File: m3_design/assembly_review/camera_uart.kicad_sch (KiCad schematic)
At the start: 13 parts, among them U12 TXU0202DCUR, U13 TPS70933DBVR

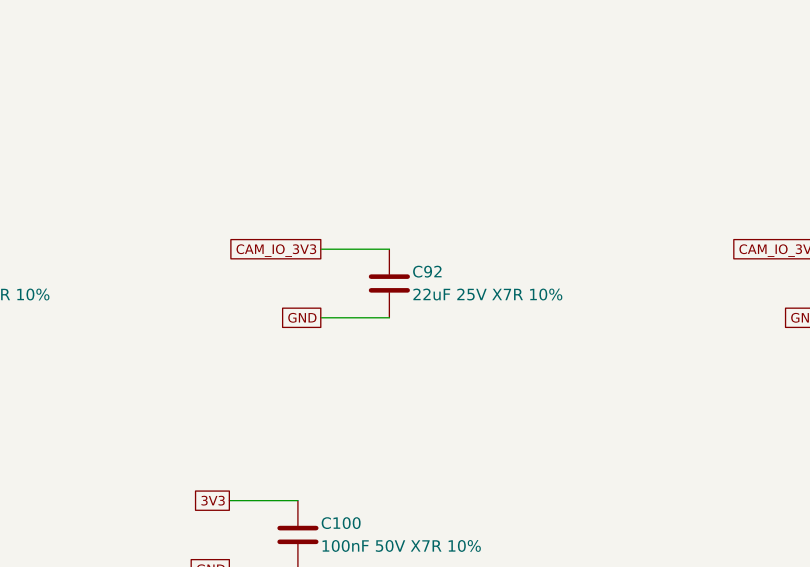
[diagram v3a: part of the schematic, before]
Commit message: R10 requirements-audit cuts and GAP fixes before review round 9
Implement adopted AUD-1 through AUD-10 and GAP-1 through GAP-5 after the single-switch pass.
Remove the advisory pull-pin, redundant probes and GPS/radio IO LDO cells; qualify the smaller
AONR21357 pair, correct C120 voltage rating, standardize shared-code capacitor lands, simplify
slow returns and fire-only copper, localize U9 output protection and add exactly two U401 VIPPO vias.
Record physical-current timing, coupled fire/source budget, C84 manual fitting and narrowed gate scopes.

Board SHA-256: 877d01996a59e9dd5c6dbc367274bb9a323a13982d67960fe46df9b0ee53205d
Board: 46 x 90 mm, 4 layers, 2365477 bytes; 225 footprints, 883 straight tracks, 323 vias.
Netlist SHA-256: 0843da709e2d7a757e9b35cdff48158a54012c5353619cbf409ab961efd2c3ca
Two fresh complete passing builds are byte-identical. Schematic: 700 pins; 22 seeded faults detected.

Final unskipped tools/check.sh: exit 0
DRC violations 0  unconnected 0  schematic parity 0  ERC 0
metadata / 3D model audit: OK
silkscreen outside the board outline: 0 stroke points
fit check: OK (CAD envelopes only)
R10 CAD contract (full): OK
routing hygiene: 0 failing, 0 allowlisted, 0 leftovers recorded
actuator safety contract: OK
Fab manifest: OK; 5 outputs match current CAD and export inputs
Self-tests: shell 4, fit 24, paste 5, routing 59, R10 131; three NumPy cases rerun and passed.

Fab: 215 CPL rows, 82 BOM codes; orientation / paste / manifest pass. Hot-plug: 2304 required
cases plus convergence and controls pass (simulation / Inference). Plate f1 280.9 Hz (Inference).
Live JLC: $84.43 vs $84.41 target, 46 Extended codes; R430 / U4 short. Procurement exit 1 is a
disclosed OQ-3 / ordering deviation, not a CAD gate pass. No quote accepted or order placed.
Firmware, bench, thermal/transient correlation, process acceptance, installed RF immunity and physical fit unverified.

This preparatory pass earns no clean-review credit. Start fresh full ten-lens round 9 on th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
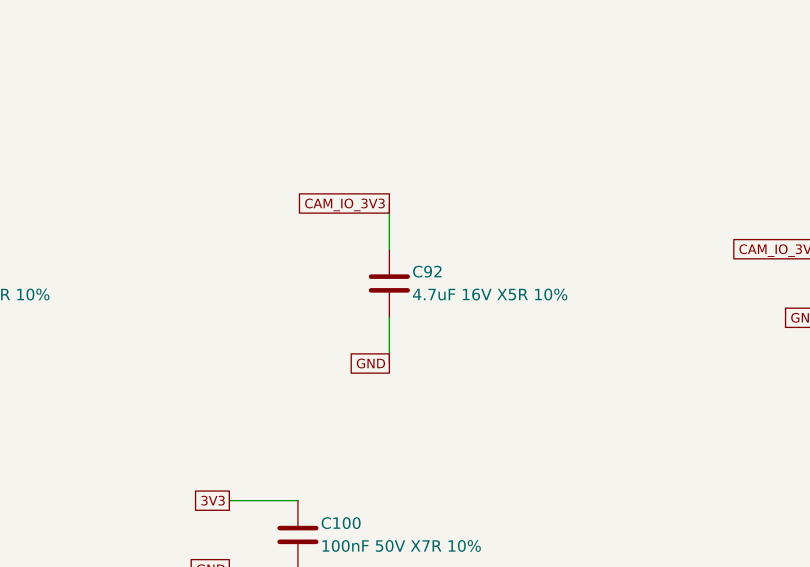
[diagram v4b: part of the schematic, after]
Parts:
- C92: value 22uF 25V X7R 10% -> 4.7uF 16V X5R 10%; footprint rocket:M3_GRM32_1210 -> rocket:C0603; LCSC C21397 -> C19666; LCSC Part C21397 -> (none); Manufacturer Murata -> Samsung Electro-Mechanics; Manufacturer Part GRM32ER71E226KE15L -> CL10A475KO8NNNC
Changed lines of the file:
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@@
+	(symbol
+		(lib_id "M3:C")
+		(at 269.24 137.16 0)
+		(unit 1)
+		(in_bom yes)
+		(on_board yes)
+		(dnp no)
+		(property "Reference" "C93"
+			(at 271.78000000000003 135.89 0)
+			(effects
+				(font
+					(size 1.27 1.27))
+				(justify left)))
+		(property "Value" "100nF 50V X7R 10%"
+			(at 271.78000000000003 138.42999999999998 0)
+			(effects
+				(font
+					(size 1.27 1.27))
+				(justify left)))
+		(property "Footprint" "rocket:C_0603_1608Metric"
+			(at 269.24 137.16 0)
+			(hide yes)
+			(effects
+				(font
+					(size 1.27 1.27))
+				(justify left)))
+		(property "Datasheet" ""
+			(at 269.24 137.16 0)
+			(hide yes)
+			(effects
+				(font
+					(size 1.27 1.27))
+				(justify left)))
+		(property "LCSC" "C14663"
+			(at 269.24 137.16 0)
+			(hide yes)
+			(effects
+				(font
+					(size 1.27 1.27))
+				(justify left)))
+		(instances
+			(project "m3"
+				(path "/6007a7db-6a58-5660-8beb-956dea045ff8/3918f78b-b8e6-50fb-8165-8fdc93a836ab"
+					(reference "C93")
+					(unit 1))))
+		(property "Manufacturer" "YAGEO"
+			(at 269.24 137.16 0)
+			(hide yes)
+			(effects
+				(font
+					(size 1.27 1.27))))
+		(property "Manufacturer Part" "CC0603KRX7R9BB104"
+			(at 269.24 137.16 0)
+			(hide yes)
+			(effects
+				(font
+					(size 1.27 1.27))))
+		(property "LCSC Part" "C14663"
+			(at 269.24 137.16 0)
+			(hide yes)
+			(effects
+				(font
+					(size 1.27 1.27)))))
+	(wire
+		(pts
+			(xy 269.24 133.35)
+			(xy 261.62 133.35))
+		(stroke
+			(width 0)
+			(type default))
+)
+	(global_label "CAM_IO_3V3"
+		(shape passive)
+		(at 261.62 133.35 0)
+		(effects
+			(font
+				(size 1.05 1.05))
+			(justify right))
+)
+	(wire
+		(pts
+			(xy 269.24 140.97)
+			(xy 261.62 140.97))
+		(stroke
+			(width 0)
+			(type default))
+)
+	(global_label "GND"
+		(shape passive)
+		(at 261.62 140.97 0)
+		(effects
+			(font
+				(size 1.05 1.05))
+			(justify right))
+)
+	(text "R8: PE8/pin38 UART7_TX and PE7/pin37 UART7_RX use AF7, no flow control (never AF7 on PE9 or PE10); off the ROM loader's USART3. PA7/pin31 controls OE as GPIO."
+		(at 20.32 231.14 0)
+		(effects
+			(font
+				(size 1.05 1.05))
+			(justify left))
+)
+	(text "U12 A-port=MCU3V3. B-port=U13 camera-derived3V3. Never substitute CAM5V for VCCB."
+		(at 20.32 237.48999999999998 0)
+		(effects
+			(font
+				(size 1.05 1.05))
+			(justify left))
+)
+	(text "Reset: R102 holds OE LOW. Set TX idle HIGH before OE; disable OE before power-down."
+		(at 20.32 243.83999999999997 0)
+		(effects
+			(font
+				(size 1.05 1.05))
+			(justify left))
+)
+	(text "U13 EN is internally biased: leave pin3 OPEN, not tied to IN. Pin4 is NC."
+		(at 20.32 250.19 0)
+		(effects
+			(font
+				(size 1.05 1.05))
+			(justify left))
+)
+	(text "UART is 3.3V, not RS232. TXU input operating range0..5.5V is not a cable battery-short rating."
+		(at 20.32 256.53999999999996 0)
+		(effects
+			(font
+				(size 1.05 1.05))
+			(justify left))
+)
+	(text "Camera VIH/VIL/VOH/VOL and timing remain unmeasured. Verify at TP75/76/90 before qualification."
+		(at 20.32 262.89 0)
+		(effects
+			(font
+				(size 1.05 1.05))
+			(justify left))
+)
+	(text "Existing v0.2 bench firmware keeps camera OFF and does not operate this UART. Full system incomplete."
+		(at 20.32 269.24 0)
+		(effects
+			(font
+				(size 1.05 1.05))
+			(justify left))
+)
 	(symbol
 		(lib_id "M3:C")
@@
 					(size 1.27 1.27))
 				(justify left)))
-		(property "Value" "22uF 25V X7R 10%"
-			(at 93.98 138.42999999999998 0)
-			(effects
-				(font
-					(size 1.27 1.27))
-				(justify left)))
-		(property "Footprint" "rocket:M3_GRM32_1210"
-			(at 91.44 137.16 0)
-			(hide yes)
-			(effects
-				(font
-					(size 1.27 1.27))
-				(justify left)))
-		(property "Datasheet" ""
-			(at 91.44 137.16 0)
-			(hide yes)
-			(effects
-				(font
-					(size 1.27 1.27))
-				(justify left)))
-		(property "LCSC" "C21397"
+		(property "Value" "4.7uF 16V X5R 10%"
+			(at 93.98 138.43 0)
+			(effects
+				(font
+					(size 1.27 1.27))
+				(justify left)))
+		(property "Footprint" "rocket:C0603"
+			(at 91.44 137.16 0)
+			(hide yes)
+			(effects
+				(font
+					(size 1.27 1.27))
+				(justify left)))
+		(property "Datasheet" "https://product.samsungsem.com/mlcc/CL10A475KO8NNN.do"
+			(at 91.44 137.16 0)
+			(hide yes)
+			(effects
+				(font
+					(size 1.27 1.27))
+				(justify left)))
+		(property "LCSC" "C19666"
+			(at 91.44 137.16 0)
+			(hide yes)
+			(effects
+				(font
+					(size 1.27 1.27))
+				(justify left)))
+		(property "Manufacturer" "Samsung Electro-Mechanics"
+			(at 91.44 137.16 0)
+			(hide yes)
+			(effects
+				(font
+					(size 1.27 1.27))
+				(justify left)))
+		(property "Manufacturer Part" "CL10A475KO8NNNC"
 			(at 91.44 137.16 0)
 			(hide yes)
@@
 				(path "/6007a7db-6a58-5660-8beb-956dea045ff8/3918f78b-b8e6-50fb-8165-8fdc93a836ab"
 					(reference "C92")
-					(unit 1))))
-		(property "Manufacturer" "Murata"
-			(at 91.44 137.16 0)
-			(hide yes)
-			(effects
-				(font
-					(size 1.27 1.27))))
-		(property "Manufacturer Part" "GRM32ER71E226KE15L"
-			(at 91.44 137.16 0)
-			(hide yes)
-			(effects
-				(font
-					(size 1.27 1.27))))
-		(property "LCSC Part" "C21397"
-			(at 91.44 137.16 0)
-			(hide yes)
-			(effects
-				(font
-					(size 1.27 1.27)))))
+					(unit 1)))))
 	(wire
 		(pts
 			(xy 91.44 133.35)
-			(xy 83.82 133.35))
+			(xy 91.44 128.27))
 		(stroke
 			(width 0)
@@
 	(global_label "CAM_IO_3V3"
 		(shape passive)
-		(at 83.82 133.35 0)
+		(at 91.44 128.27 0)
 		(effects
 			(font
@@
 		(pts
 			(xy 91.44 140.97)
-			(xy 83.82 140.97))
+			(xy 91.44 146.05))
 		(stroke
 			(width 0)
@@
 	(global_label "GND"
 		(shape passive)
-		(at 83.82 140.97 0)
+		(at 91.44 146.05 0)
 		(effects
 			(font
@@
 )
 	(symbol
-		(lib_id "M3:C")
-		(at 269.24 137.16 0)
-		(unit 1)
-		(in_bom yes)
-		(on_board yes)
-		(dnp no)
-		(property "Reference" "C93"
-			(at 271.78000000000003 135.89 0)
-			(effects
-				(font
-					(size 1.27 1.27))
-				(justify left)))
-		(property "Value" "100nF 50V X7R 10%"
-			(at 271.78000000000003 138.42999999999998 0)
-			(effects
-				(font
-					(size 1.27 1.27))
-				(justify left)))
-		(property "Footprint" "rocket:C_0603_1608Metric"
-			(at 269.24 137.16 0)
-			(hide yes)
-			(effects
-				(font
-					(size 1.27 1.27))
-				(justify left)))
-		(property "Datasheet" ""
-			(at 269.24 137.16 0)
-			(hide yes)
-			(effects
-				(font
-					(size 1.27 1.27))
-				(justify left)))
-		(property "LCSC" "C14663"
-			(at 269.24 137.16 0)
-			(hide yes)
-			(effects
-				(font
-					(size 1.27 1.27))
-				(justify left)))
-		(instances
-			(project "m3"
-				(path "/6007a7db-6a58-5660-8beb-956dea045ff8/3918f78b-b8e6-50fb-8165-8fdc93a836ab"
-					(reference "C93")
-					(unit 1))))
-		(property "Manufacturer" "YAGEO"
-			(at 269.24 137.16 0)
-			(hide yes)
-			(effects
-				(font
-					(size 1.27 1.27))))
-		(property "Manufacturer Part" "CC0603KRX7R9BB104"
-			(at 269.24 137.16 0)
-			(hide yes)
-			(effects
-				(font
-					(size 1.27 1.27))))
-		(property "LCSC Part" "C14663"
-			(at 269.24 137.16 0)
-			(hide yes)
-			(effects
-				(font
-					(size 1.27 1.27)))))
-	(wire
-		(pts
-			(xy 269.24 133.35)
-			(xy 261.62 133.35))
-		(stroke
-			(width 0)
-			(type default))
-)
-	(global_label "CAM_IO_3V3"
-		(shape passive)
-		(at 261.62 133.35 0)
-		(effects
-			(font
-				(size 1.05 1.05))
-			(justify right))
-)
-	(wire
-		(pts
-			(xy 269.24 140.97)
-			(xy 261.62 140.97))
-		(stroke
-			(width 0)
-			(type default))
-)
-	(global_label "GND"
-		(shape passive)
-		(at 261.62 140.97 0)
-		(effects
-			(font
-				(size 1.05 1.05))
-			(justify right))
-)
-	(text "R8: PE8/pin38 UART7_TX and PE7/pin37 UART7_RX use AF7, no flow control (never AF7 on PE9 or PE10); off the ROM loader's USART3. PA7/pin31 controls OE as GPIO."
-		(at 20.32 231.14 0)
-		(effects
-			(font
-				(size 1.05 1.05))
-			(justify left))
-)
-	(text "U12 A-port=MCU3V3. B-port=U13 camera-derived3V3. Never substitute CAM5V for VCCB."
-		(at 20.32 237.48999999999998 0)
-		(effects
-			(font
-				(size 1.05 1.05))
-			(justify left))
-)
-	(text "Reset: R102 holds OE LOW. Set TX idle HIGH before OE; disable OE before power-down."
-		(at 20.32 243.83999999999997 0)
-		(effects
-			(font
-				(size 1.05 1.05))
-			(justify left))
-)
-	(text "U13 EN is internally biased: leave pin3 OPEN, not tied to IN. Pin4 is NC."
-		(at 20.32 250.19 0)
-		(effects
-			(font
-				(size 1.05 1.05))
-			(justify left))
-)
-	(text "UART is 3.3V, not RS232. TXU input operating range0..5.5V is not a cable battery-short rating."
-		(at 20.32 256.53999999999996 0)
-		(effects
-			(font
-				(size 1.05 1.05))
-			(justify left))
-)
-	(text "Camera VIH/VIL/VOH/VOL and timing remain unmeasured. Verify at TP75/76/90 before qualification."
-		(at 20.32 262.89 0)
-		(effects
-			(font
-				(size 1.05 1.05))
-			(justify left))
-)
-	(text "Existing v0.2 bench firmware keeps camera OFF and does not operate this UART. Full system incomplete."
-		(at 20.32 269.24 0)
-		(effects
-			(font
-				(size 1.05 1.05))
-			(justify left))
-)
-	(symbol
